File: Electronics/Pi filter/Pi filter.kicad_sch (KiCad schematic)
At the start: 6 parts

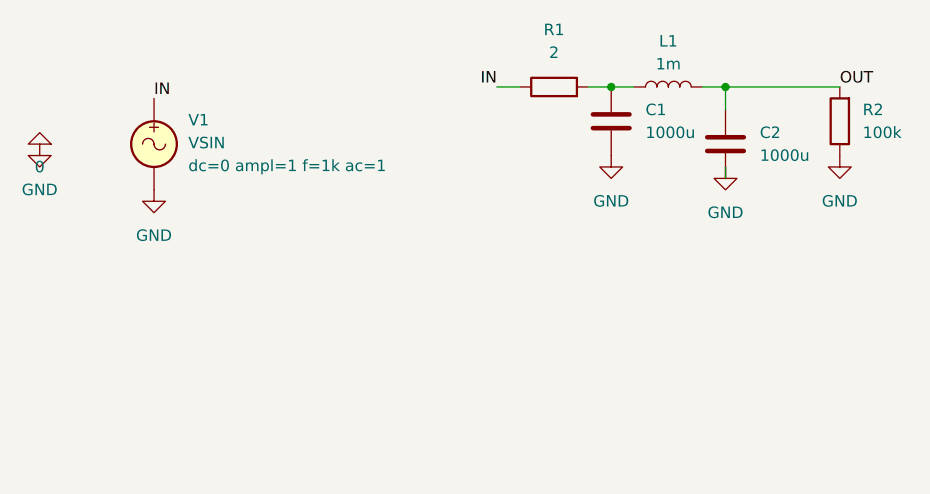
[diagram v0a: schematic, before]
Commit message: Test different power filter tradeoffs
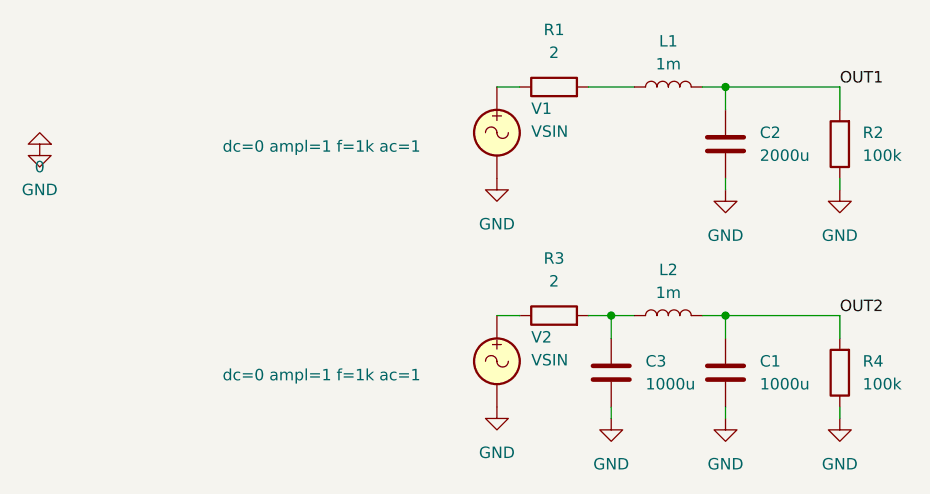
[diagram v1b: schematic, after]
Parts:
- added C3: 1000u, symbol Device:C
- added L2: 1m, symbol Device:L
- added R3: 2, symbol Device:R
- added R4: 100k, symbol Device:R
- added V2: VSIN, symbol Simulation_SPICE:VSIN
- C2: value 1000u -> 2000u
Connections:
- net 0: now also C1.1, C2.1, C3.1, R4.1, V2.2; no longer C1.2, C2.2
- net at L1.1, R1.2: no longer C1.1
- net IN: no longer names the net of R1.1, V1.1
- net OUT renamed OUT1
- net OUT1: now also C2.2; no longer C2.1
- new net: C3.2, L2.1, R3.2
- new net: R3.1, V2.1
- new net OUT2: C1.2, L2.2, R4.2
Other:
- moved on the sheet: C2, R2, V1
